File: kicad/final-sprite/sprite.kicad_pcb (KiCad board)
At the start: 4 copper layers, 35 x 44.6 mm, 63 parts, among them J1 M20-7910442R, U1 CC430F513X, U2 LSM9DS1, U3 SPRITETCXO_TCXO_7Z, U4 DRV8837, U5 ADP5092, U6 DRV8837, U7 DRV8837, X1 SPRITEPIN_SPRITE_PIN, X2 SPRITEPIN_SPRITE_PIN

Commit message: Update values from schematic
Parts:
- R1: value 47K -> 43K
- R15: value R-US_R0402 -> 5.49M
- R16: value R-US_R0402 -> 453K
- R17: value R-US_R0402 -> 4.53M
- R18: value 5.49M -> 5M
- R19: value 4.53M -> 5M
- R7: value 130K -> 150K
- R8: value 910K -> 1M
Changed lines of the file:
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@@
-(kicad_pcb (version 20171130) (host pcbnew "(5.0.0-rc2-92-g9552e0272)")
+(kicad_pcb (version 20171130) (host pcbnew "(5.0.0-rc2-216-gb0b5d9139)")
   (general
     (thickness 0.7874)
@@
       (drillshape 0)
       (scaleselection 1)
-      (outputdirectory output/))
+      (outputdirectory "output/"))
   )
   (net 0 "")
@@
       (effects (font (size 1.2065 1.2065) (thickness 0.1016)) (justify left bottom mirror))
     )
-    (fp_text value R-US_R0402 (at -0.635 -1.905 90) (layer B.Fab)
+    (fp_text value 4.53M (at -0.635 -1.905 90) (layer B.Fab)
       (effects (font (size 1.2065 1.2065) (thickness 0.1016)) (justify left bottom mirror))
     )
@@
       (effects (font (size 1 1) (thickness 0.1)) (justify left bottom mirror))
     )
-    (fp_text value 4.53M (at -0.635 -1.905 90) (layer B.Fab)
+    (fp_text value 5M (at -0.635 -1.905 90) (layer B.Fab)
       (effects (font (size 1.2065 1.2065) (thickness 0.1016)) (justify left bottom mirror))
     )
@@
       (effects (font (size 1.2065 1.2065) (thickness 0.1016)) (justify left bottom))
     )
-    (fp_text value 130K (at -0.635 1.905 270) (layer F.Fab)
+    (fp_text value 150K (at -0.635 1.905 270) (layer F.Fab)
       (effects (font (size 1.2065 1.2065) (thickness 0.1016)) (justify left bottom))
     )
@@
       (effects (font (size 1.2065 1.2065) (thickness 0.1016)) (justify left bottom))
     )
-    (fp_text value 47K (at -0.635 1.905 180) (layer F.Fab)
+    (fp_text value 43K (at -0.635 1.905 180) (layer F.Fab)
       (effects (font (size 1.2065 1.2065) (thickness 0.1016)) (justify left bottom))
     )
@@
       (effects (font (size 1 1) (thickness 0.1)) (justify left bottom mirror))
     )
-    (fp_text value 5.49M (at -0.635 -1.905 90) (layer B.Fab)
+    (fp_text value 5M (at -0.635 -1.905 90) (layer B.Fab)
       (effects (font (size 1.2065 1.2065) (thickness 0.1016)) (justify left bottom mirror))
     )
@@
       (effects (font (size 1.2065 1.2065) (thickness 0.1016)) (justify left bottom))
     )
-    (fp_text value 910K (at -0.635 1.905 90) (layer F.Fab)
+    (fp_text value 1M (at -0.635 1.905 90) (layer F.Fab)
       (effects (font (size 1.2065 1.2065) (thickness 0.1016)) (justify left bottom))
     )
@@
       (effects (font (size 1.2065 1.2065) (thickness 0.1016)) (justify left bottom mirror))
     )
-    (fp_text value R-US_R0402 (at -0.635 -1.905 270) (layer B.Fab)
+    (fp_text value 453K (at -0.635 -1.905 270) (layer B.Fab)
       (effects (font (size 1.2065 1.2065) (thickness 0.1016)) (justify left bottom mirror))
     )
@@
       (effects (font (size 1.2065 1.2065) (thickness 0.1016)) (justify left bottom mirror))
     )
-    (fp_text value R-US_R0402 (at -0.635 -1.905 270) (layer B.Fab)
+    (fp_text value 5.49M (at -0.635 -1.905 270) (layer B.Fab)
       (effects (font (size 1.2065 1.2065) (thickness 0.1016)) (justify left bottom mirror))
     )
@@
     (pad "" np_thru_hole circle (at 0 0) (size 2.8 2.8) (drill 2.8) (layers *.Cu *.Mask))
   )
-  (module sprite:logo (layer Top)
+  (module sprite:logo locked (layer Top)
     (at 142.494 96.012)
     (fp_text reference G*** (at 0 0) (layer F.SilkS) hide

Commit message: Update fab drawing
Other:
- board text added: "NOTES: 1. MATERIAL: STANDARD 4-LAYER FR4 STACKUP, 0.031" OVERALL THICKNESS. 1 OZ COPPER ON ALL LAYERS. 2. FINISH: ELECTROLESS NICKEL IMMERSION GOLD (ENIG) 3. SOLDERMASK: TENT ALL VIAS. COLOR: BLACK MATTE OR LEAST EXPENSIVE OPTION. 4. TRIM COPPER AROUND BOARD EDGE AS NEEDED TO FABRICATE WITH STANDARD CAPABILITY. 5. MANUFACTURE WITH STANDARD CAPABILITIES. EXCEPT DESIGN RULES AS INDICATED."
- board text removed: "STACKUP: STANDARD FR4. 31 MIL OVERALL THICKNESS. 1.5 OZ COPPER OUTER LAYERS. 1.0 OZ COPPER INNER LAYERS. FINISH: ENIG TENT ALL VIAS TRIM COPPER AROUND BOARD EDGE AS NEEDED TO FABRICATE WITH STANDARD CAPABILITY."
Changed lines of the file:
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@@
   (gr_line (start 151.8411 108.152074) (end 155.8411 108.152074) (layer Edge.Cuts) (width 0.15))
   (gr_arc (start 155.321 109.1692) (end 155.321 108.1532) (angle -126.9) (layer Cmts.User) (width 0.15))
-  (gr_text "STACKUP:\nSTANDARD FR4.\n31 MIL OVERALL THICKNESS.\n1.5 OZ COPPER OUTER LAYERS.\n1.0 OZ COPPER INNER LAYERS.\n\nFINISH: ENIG\n\nTENT ALL VIAS\n\nTRIM COPPER AROUND BOARD\nEDGE AS NEEDED TO FABRICATE\nWITH STANDARD CAPABILITY." (at 78.232 96.52) (layer Cmts.User)
+  (gr_text "NOTES:\n\n 1. MATERIAL: STANDARD 4-LAYER FR4 STACKUP, 0.031\" OVERALL THICKNESS.\n    1 OZ COPPER ON ALL LAYERS.\n\n 2. FINISH: ELECTROLESS NICKEL IMMERSION GOLD (ENIG)\n\n 3. SOLDERMASK: TENT ALL VIAS. COLOR: BLACK MATTE OR LEAST EXPENSIVE OPTION.\n\n 4. TRIM COPPER AROUND BOARD EDGE AS NEEDED TO FABRICATE\n    WITH STANDARD CAPABILITY.\n\n 5. MANUFACTURE WITH STANDARD CAPABILITIES. EXCEPT DESIGN RULES AS INDICATED." (at 15.24 97.79) (layer Cmts.User)
     (effects (font (size 1.5 1.5) (thickness 0.3)) (justify left))
   )

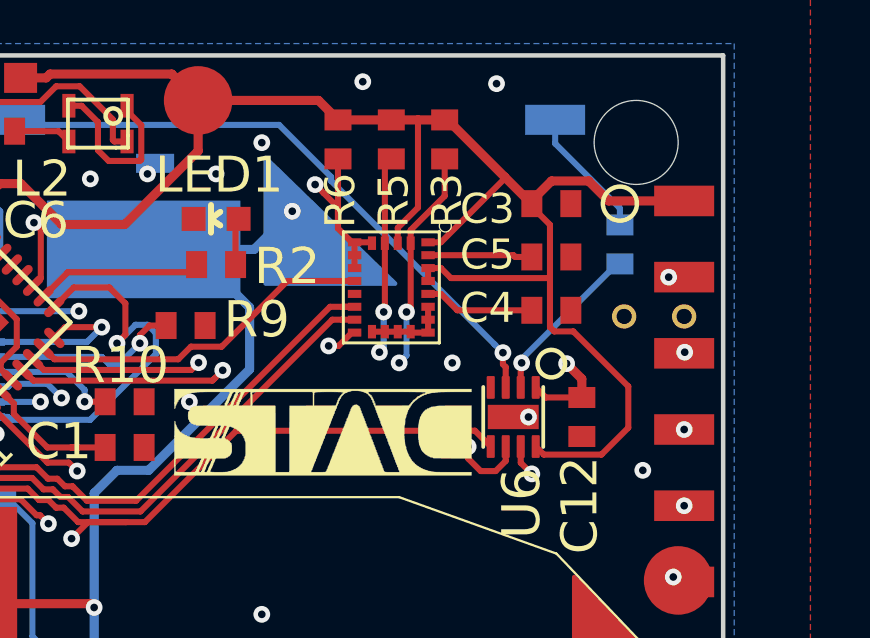
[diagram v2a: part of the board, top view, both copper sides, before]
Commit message: Add ground vias
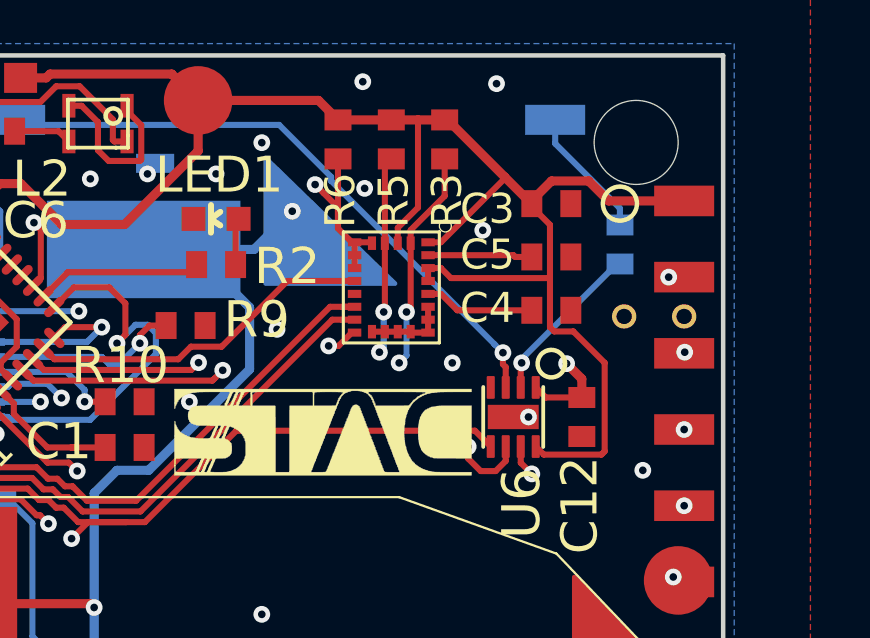
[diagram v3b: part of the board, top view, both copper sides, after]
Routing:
- net VCC: track 138.3 -> 137.6 mm
- net GND: vias 27 -> 30
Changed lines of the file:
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@@
-(kicad_pcb (version 20171130) (host pcbnew "(5.0.0-rc2-216-gb0b5d9139)")
+(kicad_pcb (version 20171130) (host pcbnew "(5.0.0-rc2-225-g4af699e91)")
   (general
     (thickness 0.7874)
     (drawings 26)
-    (tracks 959)
+    (tracks 962)
     (zones 0)
     (modules 63)
@@
     (pad_to_mask_clearance 0.2)
     (aux_axis_origin 0 0)
-    (visible_elements FFFFFFFF)
+    (visible_elements FFF9FFFF)
     (pcbplotparams
       (layerselection 0x012f0_ffffffff)
@@
   (segment (start 146.4332 90.541) (end 146.766201 90.874001) (width 0.2032) (layer Top) (net 1))
   (segment (start 146.005 90.541) (end 146.4332 90.541) (width 0.2032) (layer Top) (net 1) (status 10))
-  (segment (start 150.068001 92.509203) (end 150.068001 90.823201) (width 0.2032) (layer Top) (net 1))
-  (segment (start 150.210799 92.652001) (end 150.068001 92.509203) (width 0.2032) (layer Top) (net 1))
-  (segment (start 150.845435 92.652001) (end 150.210799 92.652001) (width 0.2032) (layer Top) (net 1))
-  (segment (start 152.679401 94.485967) (end 150.845435 92.652001) (width 0.2032) (layer Top) (net 1))
-  (segment (start 152.679401 95.861801) (end 152.679401 94.485967) (width 0.2032) (layer Top) (net 1))
-  (segment (start 151.783201 96.758001) (end 152.679401 95.861801) (width 0.2032) (layer Top) (net 1))
-  (segment (start 149.863001 96.758001) (end 151.783201 96.758001) (width 0.2032) (layer Top) (net 1))
-  (segment (start 149.594 96.489) (end 149.863001 96.758001) (width 0.2032) (layer Top) (net 1) (status 10))
   (segment (start 123.22 98.135998) (end 122.361999 98.993999) (width 0.2032) (layer Top) (net 1))
   (segment (start 123.22 97.155) (end 123.22 98.135998) (width 0.2032) (layer Top) (net 1) (status 10))
@@
   (segment (start 133.2768 84.201) (end 133.40466 84.07314) (width 0.3048) (layer Top) (net 1))
   (segment (start 132.422 84.201) (end 133.2768 84.201) (width 0.3048) (layer Top) (net 1))
+  (segment (start 150.068001 92.509203) (end 150.068001 90.823201) (width 0.2032) (layer Top) (net 1))
+  (segment (start 150.210799 92.652001) (end 150.068001 92.509203) (width 0.2032) (layer Top) (net 1))
+  (segment (start 150.845435 92.652001) (end 150.210799 92.652001) (width 0.2032) (layer Top) (net 1))
+  (segment (start 149.594 96.489) (end 149.863001 96.758001) (width 0.2032) (layer Top) (net 1))
+  (segment (start 151.892 93.698566) (end 150.845435 92.652001) (width 0.2032) (layer Top) (net 1))
+  (segment (start 151.892 96.649202) (end 151.892 93.698566) (width 0.2032) (layer Top) (net 1))
+  (segment (start 151.783201 96.758001) (end 151.892 96.649202) (width 0.2032) (layer Top) (net 1))
+  (segment (start 149.863001 96.758001) (end 151.783201 96.758001) (width 0.2032) (layer Top) (net 1))
   (via (at 154.178 100.838) (size 0.5588) (drill 0.254) (layers Top Bottom) (net 2) (status 30))
   (via (at 149.352 95.504) (size 0.5588) (drill 0.254) (layers Top Bottom) (net 2) (status 30))
@@
   (via (at 141.478 114.046) (size 0.5588) (drill 0.254) (layers Top Bottom) (net 2))
   (via (at 145.542 114.046) (size 0.5588) (drill 0.254) (layers Top Bottom) (net 2))
+  (via (at 143.891 87.884) (size 0.5588) (drill 0.254) (layers Top Bottom) (net 2))
+  (via (at 140.97 92.583) (size 0.5588) (drill 0.254) (layers Top Bottom) (net 2))
+  (via (at 147.828 89.281) (size 0.5588) (drill 0.254) (layers Top Bottom) (net 2))
   (via (at 141.478 88.646) (size 0.5588) (drill 0.254) (layers Top Bottom) (net 3) (status 30))
   (via (at 145.034 110.617) (size 0.5588) (drill 0.254) (layers Top Bottom) (net 3) (status 30))

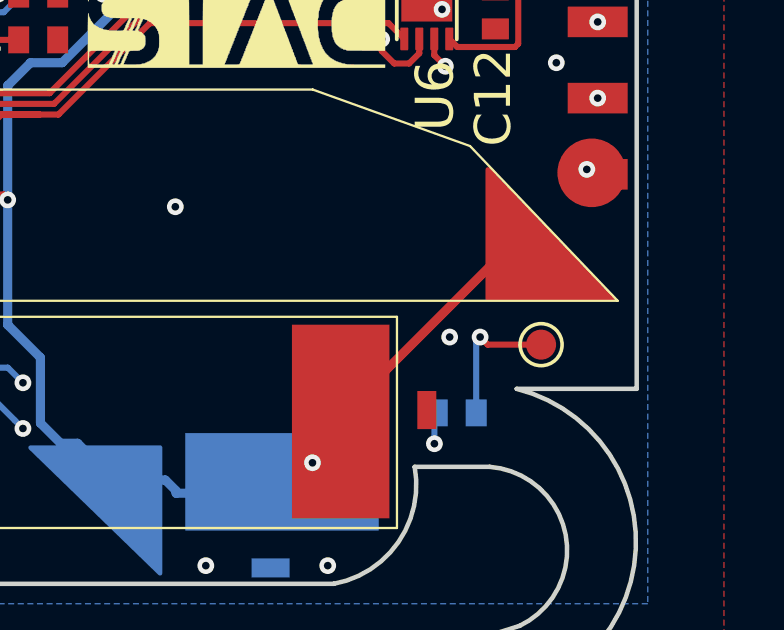
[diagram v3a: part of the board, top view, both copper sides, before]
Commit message: Fix inductor test points
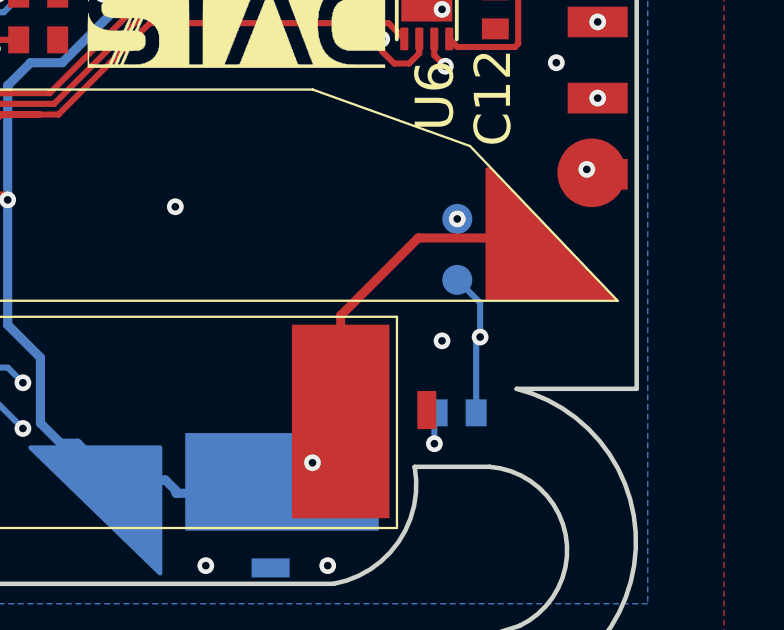
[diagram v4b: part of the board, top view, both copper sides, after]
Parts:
- added TP1: Test_Point, TestPoint:TestPoint_Pad_D1.0mm, B.Cu at (149.9, 104.5)
- TP2: moved to B.Cu
- moved TP2 5.04 mm to (149.9, 102.5), turned to 270 degrees
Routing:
- net Net-(R22-Pad1): track 732.0 -> 736.5 mm, vias 3 -> 4
- net VCCINT: track 94.2 -> 96.6 mm

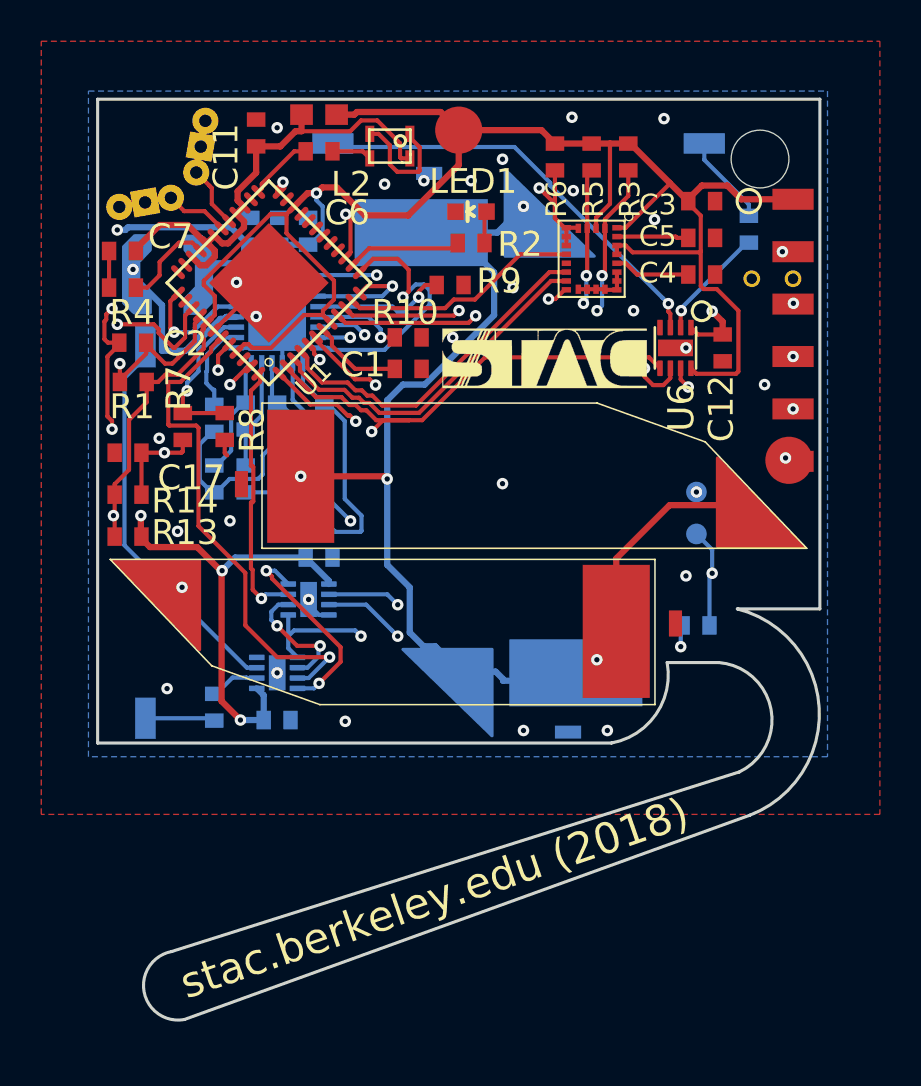
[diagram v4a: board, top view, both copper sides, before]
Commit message: Fix silkscreen
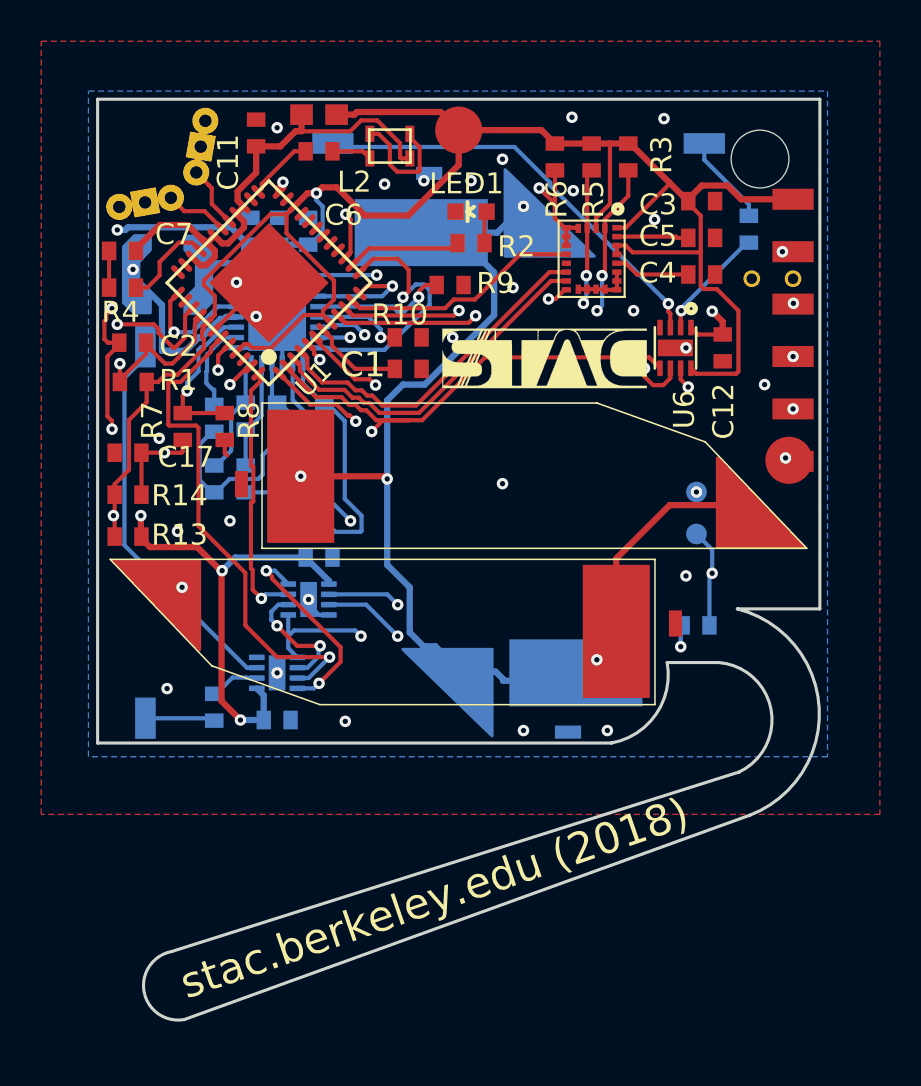
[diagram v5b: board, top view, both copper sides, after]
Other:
- board text removed: "+"
- board text removed: "-"

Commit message: Fix size of R10
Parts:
- R10: value 750K -> 200k
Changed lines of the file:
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@@
       (effects (font (size 1.016 1.016) (thickness 0.1016)) (justify left bottom))
     )
-    (fp_text value 750K (at -0.635 1.905 180) (layer F.Fab)
+    (fp_text value 200k (at -0.635 1.905 180) (layer F.Fab)
       (effects (font (size 1.2065 1.2065) (thickness 0.1016)) (justify left bottom))
     )
